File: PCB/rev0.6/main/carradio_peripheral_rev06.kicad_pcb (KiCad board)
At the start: 4 copper layers, 100 x 100 mm, 213 parts, among them J1 ISO 10487 A (via pigtail), J10 K-line module socket, J12 Display buttons, J13 HDMI in (from VIM3), J14 Display FPC 40P 0.5mm, J18 VIM3 VIN (JST-XH 2P), J2 VIM3 40-pin via 2x20 IDC ribb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, J21 Expansion 2, J22 SWD, J23 Audio module socket, J25 USB module socket, J27 GNSS module socket, J5 VIM3 POWER key lead, J7 BH1750 light sensor, J8 ISO 10487 C1 (via pigtail), Q1 AO3400A, Q10 P-MOSFET -40V, Q11 CSD18543Q3A, Q12 CSD18543Q3A, Q2 P-MOSFET -60V, Q3 2N7002, SW1 BOOTSEL, SW2 RESET, U1 TPS560430XDBVR, U12 TPS55288RPMR, U13 CH334R, U19 AP2112K-3.3, U2 EL817S1(C), U20 RP2350B, U21 W25Q128JVS, U3 EL817S1(C), U4 EL817S1(C), U5 EL817S1(C), U6 LP5907MFX-3.3, Y1 12MHz, Y3 12MHz

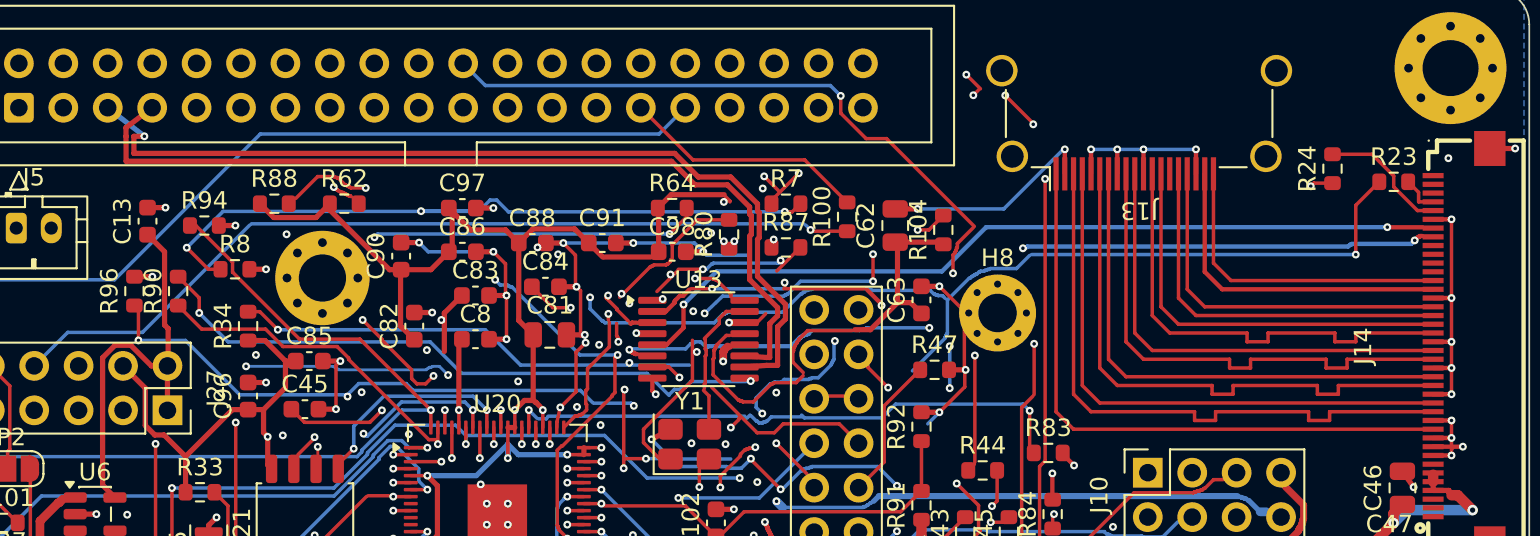
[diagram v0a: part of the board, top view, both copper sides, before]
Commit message: PCB rev 0.6: HDMI and USB_UP pairs to JLC calculator impedance
JLCPCB's impedance calculator for JLC04161H-7628 (L1 over L2):
90 ohm = 0.334/0.300 mm, 100 ohm = 0.2187/0.20 mm.

- HDMI D0-D2/CLK rebuilt (hdmipairs.py) as coupled 0.2187/0.20 mm pairs
  centred over each GND pin, with 45-degree jogs at J13/J14. Before:
  0.20 mm traces 0.80 mm apart (about 140 ohm). P/N matched to 0.69 mm.
- USB_UP re-routed at 0.32/0.30 mm (0.32 fits between U13 and J23),
  In1 keep-out rebuilt (0.5 mm, open at U13's escapes and two vias
  beside the pair).
- Net classes updated; order and fab files regenerated; docs updated.

DRC: 0 unconnected, no errors; schematic parity unchanged.

Co-Authored-By: Claude Opus 5.5 (1M context) <noreply@anthropic.com>
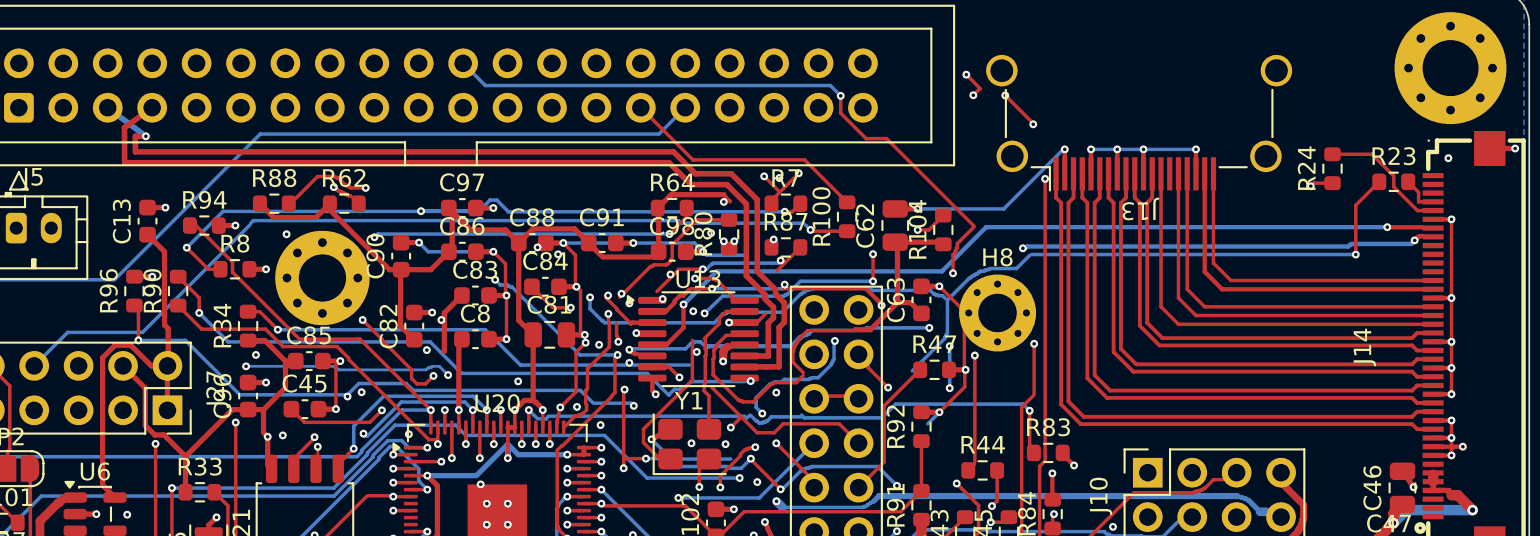
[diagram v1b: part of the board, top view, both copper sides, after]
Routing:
- net /MCU_BTN_MUTE: track 148.3 -> 150.0 mm
- net /HDMI_CLKN: track 26.6 -> 25.5 mm
- net /HDMI_D2N: track 35.6 -> 34.5 mm
- net /HDMI_D1N: track 32.6 -> 31.5 mm
- net /HDMI_D0N: track 29.6 -> 28.5 mm

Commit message: PCB rev 0.6: DFM cleanup (dangling vias, vias on pins, pad gaps), CPL files
- Removed the dangling vias and track stubs left by the routers, the
  fan-out stubs/vias on unused GPIO44-47 and zero-length segments
  (prune.py, prune2.py, prune3.py).
- 16 vias that sat in or on the edge of SMD pins moved 0.15 mm clear
  with a short stub (fixvip.py); thermal vias in exposed pads stay.
- Q11/Q12 pins 3-4 and U12 pins 7-8 trimmed 0.01 mm to meet JLC's
  0.15 mm pad-to-pad minimum (padtrim.py).
- order/ now also has *_cpl.csv and *_jlc_bom.csv per board.

DRC: 0 unconnected, no errors; schematic parity unchanged.

Co-Authored-By: Claude Opus 5.5 (1M context) <noreply@anthropic.com>
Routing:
- net /+5V_AON: track 189.6 -> 181.1 mm, vias 18 -> 17
- net /LUX_SDA: track 214.9 -> 207.8 mm
- net /VIM3_I2S_MCLK: track 60.2 -> 54.9 mm, vias 8 -> 7
- net /MCU_BL_EN: track 109.0 -> 104.1 mm
- net /MCU_USBP_FAULT1: track 57.8 -> 53.4 mm, vias 7 -> 4
- net /HUB2_UP_DM: track 49.3 -> 46.5 mm
- net /MCU_TEMP_ADC: track 44.9 -> 47.4 mm
- net /VBAT_P: track 125.7 -> 128.2 mm
- net /I2S_BCLK: track 13.4 -> 10.9 mm
- net GND: track 666.2 -> 668.4 mm
- net /MCU_SWCLK: track 64.2 -> 62.0 mm, vias 4 -> 3
- net /MCU_SWDIO: track 67.3 -> 65.5 mm
- net /MCU_BL_PWM: track 63.5 -> 61.9 mm
- net /MCU_XTAL_R: track 20.5 -> 19.0 mm
- net /+1V1_MCU: track 82.4 -> 81.1 mm, vias 7 -> 6
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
